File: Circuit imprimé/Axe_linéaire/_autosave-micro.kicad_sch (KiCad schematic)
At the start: 6 parts, among them Q1 LP2301LT1G, SW1 SW_MEC_5G, U1 PicoW

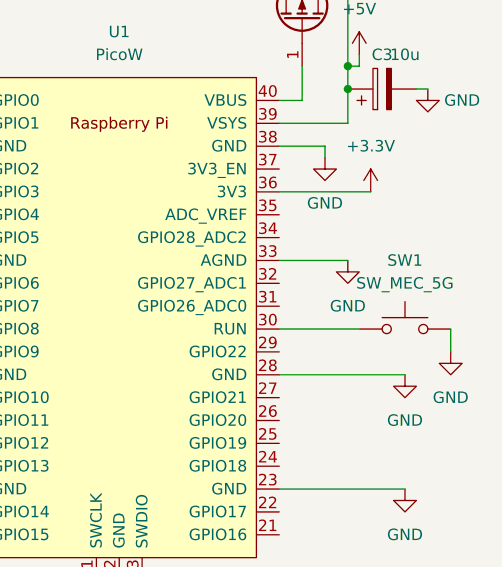
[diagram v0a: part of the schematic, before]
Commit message: Ajout de l'IMU + modèle du photointerrupteur
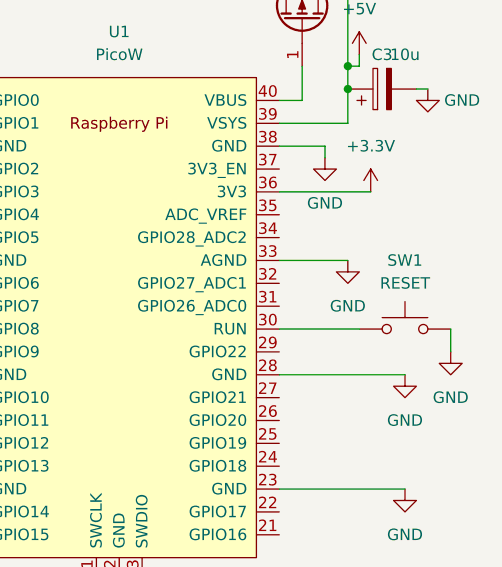
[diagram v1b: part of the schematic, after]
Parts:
- SW1: value SW_MEC_5G -> RESET
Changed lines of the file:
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@@
     (in_bom yes) (on_board yes) (fields_autoplaced)
     (property "Reference" "SW1" (id 0) (at 172.72 62.23 0))
-    (property "Value" "SW_MEC_5G" (id 1) (at 172.72 64.77 0))
+    (property "Value" "RESET" (id 1) (at 172.72 64.77 0))
     (property "Footprint" "Library:Tactile Button" (id 2) (at 172.72 64.77 0)
       (effects (font (size 1.27 1.27)) hide)
